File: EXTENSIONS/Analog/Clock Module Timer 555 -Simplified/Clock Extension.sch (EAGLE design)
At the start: 8 parts, among them T555_CLOCK NE555N, X1 USB-A

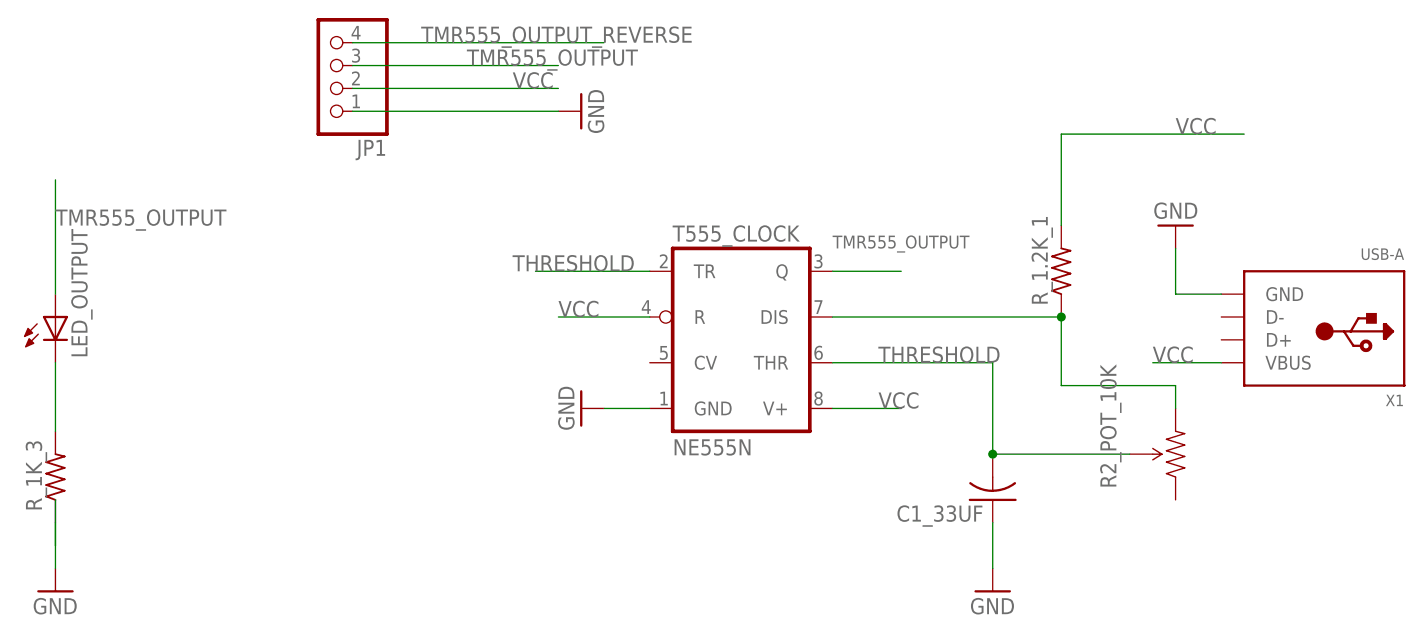
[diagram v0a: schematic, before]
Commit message: fix bug in pcb '0 TO 9 Counter 74LS90'
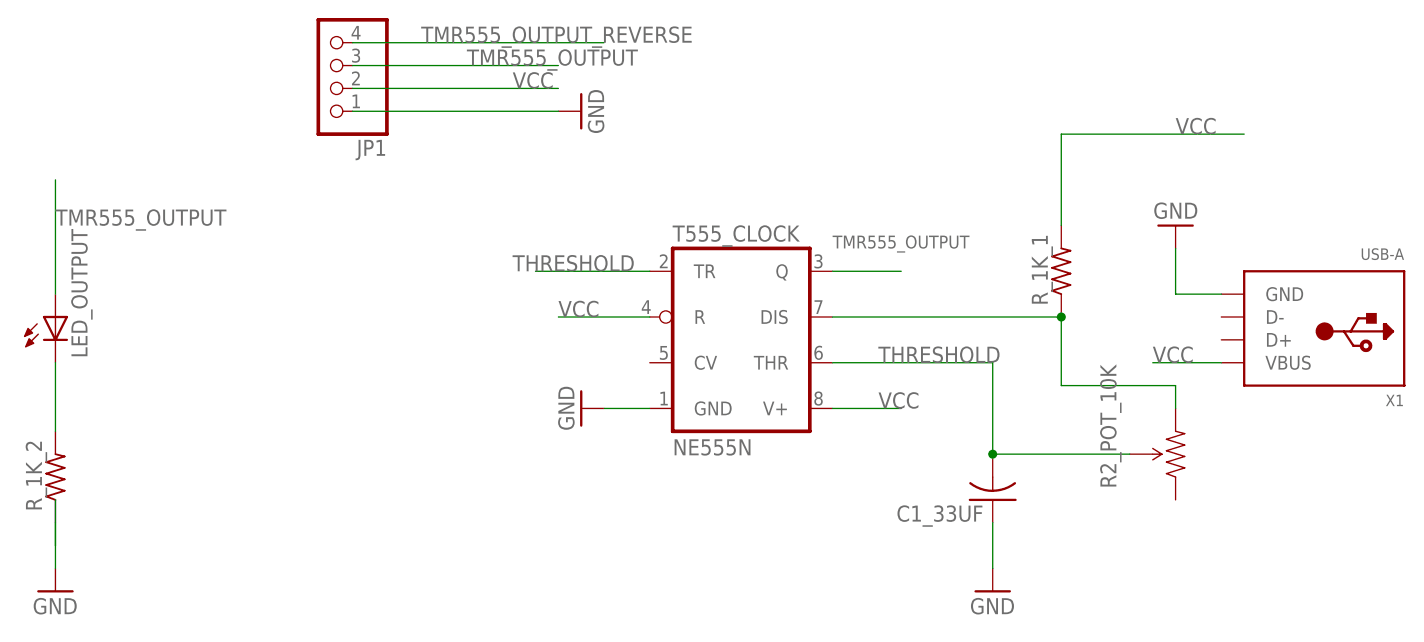
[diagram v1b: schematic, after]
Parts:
- renumbered R_1.2K_1 to R_1K_1, R_1K_3 to R_1K_2
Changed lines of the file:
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@@
 <part name="JP1" library="pinhead" deviceset="PINHD-1X4" device=""/>
 <part name="GND5" library="supply1" deviceset="GND" device=""/>
-<part name="R_1.2K_1" library="adafruit" deviceset="R-US_" device="R1206"/>
+<part name="R_1K_1" library="adafruit" deviceset="R-US_" device="R1206"/>
 <part name="R2_POT_10K" library="SparkFun-Electromechanical" deviceset="TRIMPOT" device="PTH"/>
 <part name="LED_OUTPUT" library="adafruit" deviceset="LED" device="SMT1206"/>
-<part name="R_1K_3" library="adafruit" deviceset="R-US_" device="R1206"/>
+<part name="R_1K_2" library="adafruit" deviceset="R-US_" device="R1206"/>
 <part name="GND7" library="supply1" deviceset="GND" device=""/>
 </parts>
@@
 <instance part="JP1" gate="A" x="17.78" y="127" rot="R180"/>
 <instance part="GND5" gate="1" x="45.72" y="121.92" rot="R90"/>
-<instance part="R_1.2K_1" gate="G$1" x="99.06" y="104.14" rot="R90"/>
+<instance part="R_1K_1" gate="G$1" x="99.06" y="104.14" rot="R90"/>
 <instance part="R2_POT_10K" gate="R?" x="111.76" y="83.82" smashed="yes" rot="R90">
 <attribute name="NAME" x="105.1814" y="80.01" size="1.778" layer="95" rot="R90"/>
@@
 </instance>
 <instance part="LED_OUTPUT" gate="G$1" x="-12.7" y="99.06"/>
-<instance part="R_1K_3" gate="G$1" x="-12.7" y="81.28" rot="R90"/>
+<instance part="R_1K_2" gate="G$1" x="-12.7" y="81.28" rot="R90"/>
 <instance part="GND7" gate="1" x="-12.7" y="68.58"/>
 </instances>
@@
 </segment>
 <segment>
-<pinref part="R_1K_3" gate="G$1" pin="1"/>
+<pinref part="R_1K_2" gate="G$1" pin="1"/>
 <pinref part="GND7" gate="1" pin="GND"/>
 <wire x1="-12.7" y1="76.2" x2="-12.7" y2="73.66" width="0.1524" layer="91"/>
@@
 <wire x1="99.06" y1="119.38" x2="119.38" y2="119.38" width="0.1524" layer="91"/>
 <label x="111.76" y="119.38" size="1.778" layer="95"/>
-<pinref part="R_1.2K_1" gate="G$1" pin="2"/>
+<pinref part="R_1K_1" gate="G$1" pin="2"/>
 <wire x1="99.06" y1="119.38" x2="99.06" y2="109.22" width="0.1524" layer="91"/>
 </segment>
@@
 <pinref part="T555_CLOCK" gate="A" pin="DIS"/>
 <wire x1="73.66" y1="99.06" x2="99.06" y2="99.06" width="0.1524" layer="91"/>
-<pinref part="R_1.2K_1" gate="G$1" pin="1"/>
+<pinref part="R_1K_1" gate="G$1" pin="1"/>
 <pinref part="R2_POT_10K" gate="R?" pin="CW"/>
 <wire x1="111.76" y1="88.9" x2="111.76" y2="91.44" width="0.1524" layer="91"/>
@@
 <segment>
 <pinref part="LED_OUTPUT" gate="G$1" pin="C"/>
-<pinref part="R_1K_3" gate="G$1" pin="2"/>
+<pinref part="R_1K_2" gate="G$1" pin="2"/>
 <wire x1="-12.7" y1="93.98" x2="-12.7" y2="86.36" width="0.1524" layer="91"/>
 </segment>

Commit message: Prepare for shipping to seeedstudio manufacturing
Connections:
- removed net TMR555_OUTPUT_REVERSE: JP1.4
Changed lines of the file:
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@@
-</segment>
-</net>
-<net name="TMR555_OUTPUT_REVERSE" class="0">
-<segment>
-<pinref part="JP1" gate="A" pin="4"/>
-<wire x1="20.32" y1="129.54" x2="48.26" y2="129.54" width="0.1524" layer="91"/>
-<label x="27.94" y="129.54" size="1.778" layer="95"/>
 </segment>
 </net>
